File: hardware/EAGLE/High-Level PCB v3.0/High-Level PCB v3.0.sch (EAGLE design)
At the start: 38 parts, among them IC1 DS8921, IC2 DS8921, IC3 MCP2551, J1 Micro-SD, J2 Gyro, J3 Compass, J4 GPS, J5 DB9 Plug, J6 Compass, X1 RJ45, X2 Vehicle control, X4 RJ45

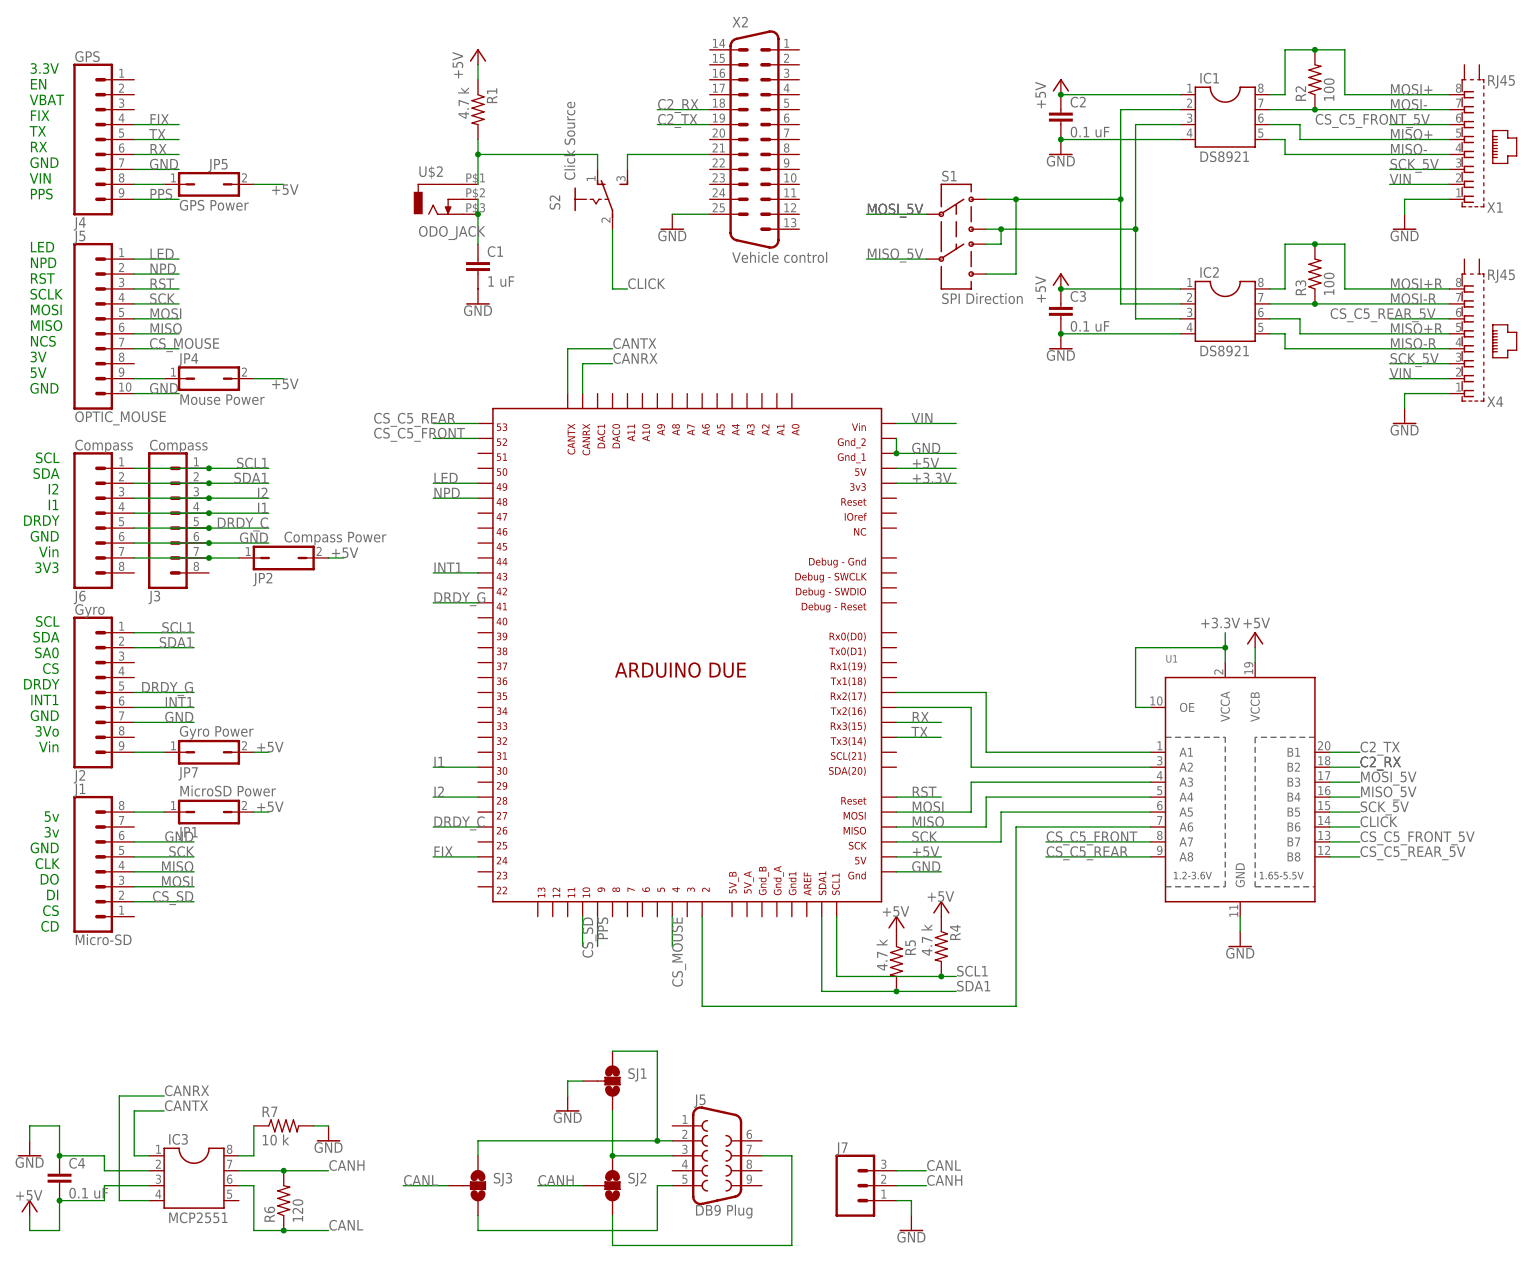
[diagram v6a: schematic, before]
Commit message: Added Test Points
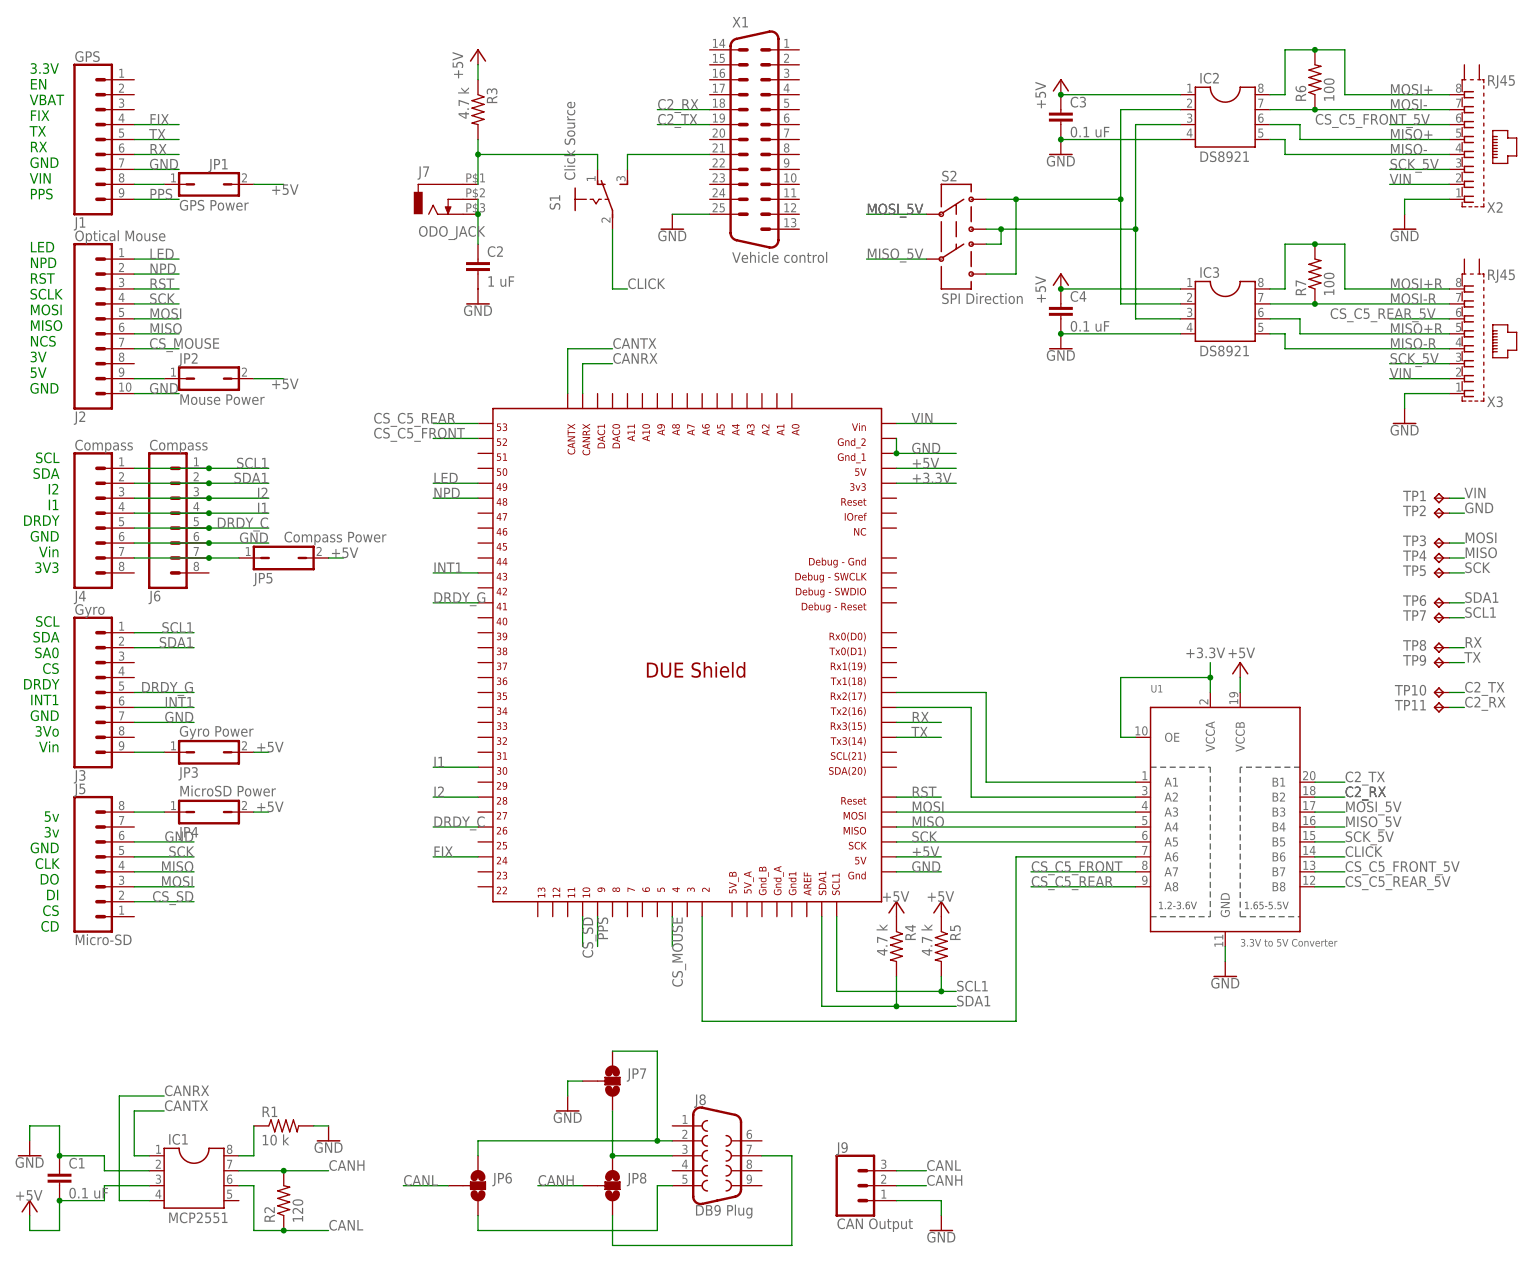
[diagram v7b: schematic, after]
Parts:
- removed OPTIC_MOUSE: J5, SparkFun-Connectors:CONN_10"
- removed SJ1: JUMPER-SMT_3_NO_SILK, SparkFun-Jumpers:JUMPER-SMT_3_NO_SILK
- removed U$2: ODO_JACK, elcanoParts:ODO_JACK
- added J8: DB9 Plug, SparkFun-Connectors:DB9MALE
- added J9: CAN Output, SparkFun-Connectors:CONN_03-SCREW-5MM
- added JP3: Gyro Power, jumper:JP1Q
- added TP1, TP10, TP11, TP2, TP3, TP4, TP5, TP6, TP7, TP8, TP9: TPPAD1-17, testpad:TPPAD1-17
- C1: value 1 uF -> 0.1 uF
- C2: value 0.1 uF -> 1 uF
- IC1: value DS8921 -> MCP2551
- IC3: value MCP2551 -> DS8921
- J1: value Micro-SD -> GPS; device SparkFun-Connectors:CONN_08" -> SparkFun-Connectors:CONN_09
- J2: value Gyro -> Optical Mouse; device SparkFun-Connectors:CONN_09 -> SparkFun-Connectors:CONN_10"
- J3: value Compass -> Gyro; device SparkFun-Connectors:CONN_08" -> SparkFun-Connectors:CONN_09
- J4: value GPS -> Compass; device SparkFun-Connectors:CONN_09 -> SparkFun-Connectors:CONN_08"
- J5: value DB9 Plug -> Micro-SD; device SparkFun-Connectors:DB9MALE -> SparkFun-Connectors:CONN_08"
- J7: value (none) -> ODO_JACK; device SparkFun-Connectors:CONN_03-SCREW-5MM -> elcanoParts:ODO_JACK
- JP1: value MicroSD Power -> GPS Power
- JP2: value Compass Power -> Mouse Power
- JP4: value Mouse Power -> MicroSD Power
- JP5: value GPS Power -> Compass Power
- JP7: value Gyro Power -> JUMPER-SMT_3_NO_SILK; device jumper:JP1Q -> SparkFun-Jumpers:JUMPER-SMT_3_NO_SILK
- R1: value 4.7 k -> 10 k; device resistor:R-US_0204/5 -> rcl:R-US_0204/5
- R2: value 100 -> 120
- R3: value 100 -> 4.7 k; device rcl:R-US_0204/5 -> resistor:R-US_0204/5
- R6: value 120 -> 100
- R7: value 10 k -> 100
- S1: value SPI Direction -> Click Source; device elcanoParts:DPDT_DEV6X5MM_PAC -> switch:255SB
- S2: value Click Source -> SPI Direction; device switch:255SB -> elcanoParts:DPDT_DEV6X5MM_PAC
- U1: value (none) -> 3.3V to 5V Converter
- X1: value RJ45 -> Vehicle control; device con-kycon:GLX-S-88M -> con-subd:M25H
- X2: value Vehicle control -> RJ45; device con-subd:M25H -> con-kycon:GLX-S-88M
- renumbered SJ2 to JP8, SJ3 to JP6, U$1 to MCU1, X4 to X3
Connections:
- removed net N$14 (its old number): J4.8, JP5.1
- new net N$10: J5.8, JP4.1
- net +5V: now also C1.2, C4.1, IC1.3, IC3.1, JP3.2, R3.1; no longer C2.1, C4.2, IC1.1, IC3.3, JP7.2, R1.1
- net C2_RX: now also TP11.TP, X1.18; no longer X2.18
- net C2_TX: now also TP10.TP, X1.19; no longer X2.19
- net CANH: now also IC1.7, J9.2, R2.2; no longer IC3.7, J7.2, R6.2
- net CANL: now also IC1.6, J9.3, R2.1; no longer IC3.6, J7.3, R6.1
- net CANRX: now also IC1.4; no longer IC3.4
- net CANTX: now also IC1.1; no longer IC3.1
- net CLICK: now also S1.P; no longer S2.P
- net CS_C5_FRONT_5V: now also X2.6; no longer X1.6
- net CS_MOUSE: now also J2.7; no longer OPTIC_MOUSE.7
- net CS_SD: now also J5.2; no longer J1.2
- net DRDY_C: now also J4.5; no longer J3.5
- net DRDY_G: now also J3.5; no longer J2.5
- net FIX: now also J1.4; no longer J4.4
- net GND: now also C1.1, C4.2, IC1.2, IC3.4, J1.7, J2.10, J3.7, J4.6, J5.6, J9.1, JP7.2, R1.2, TP2.TP, X1.25, X2.1; no longer C1.2, C4.1, IC1.4, IC3.2, J1.6, J2.7, J3.6, J4.7, J7.1, OPTIC_MOUSE.10, R7.2, SJ1.2, X1.1, X2.25
- net I1: now also J4.4; no longer J3.4
- net I2: now also J4.3; no longer J3.3
- net INT1: now also J3.6; no longer J2.6
- net LED: now also J2.1; no longer OPTIC_MOUSE.1
- net MISO: now also J2.6, J5.4, TP4.TP; no longer J1.4, OPTIC_MOUSE.6
- net MISO+: now also IC2.6, X2.5; no longer IC1.6, X1.5
- net MISO+R: now also IC3.6; no longer IC2.6
- net MISO-: now also IC2.5, X2.4; no longer IC1.5, X1.4
- net MISO-R: now also IC3.5; no longer IC2.5
- net MISO_5V: now also S2.5; no longer S1.5
- net MOSI: now also J2.5, J5.3, TP3.TP; no longer J1.3, OPTIC_MOUSE.5
- net MOSI+: now also IC2.8, R6.2, X2.8; no longer IC1.8, R2.2, X1.8
- net MOSI+R: now also IC3.8, R7.2; no longer IC2.8, R3.2
- net MOSI-: now also IC2.7, R6.1, X2.7; no longer IC1.7, R2.1, X1.7
- net MOSI-R: now also IC3.7, R7.1; no longer IC2.7, R3.1
- net MOSI_5V: now also S2.2; no longer S1.2
- net N$1: now also C2.1, J7.2, J7.3; no longer C1.1, U$2.2, U$2.3
- net N$11: now also J8.3, JP7.3; no longer J5.3, SJ1.3
- net N$13: now also J2.9, JP2.1; no longer JP4.1, OPTIC_MOUSE.9
- net N$15: now also J8.5; no longer J5.5
- net N$16: now also J8.7; no longer J5.7
- net N$17: now also IC1.8, R1.1; no longer IC3.8, R7.1
- net N$18: now also J8.2, JP7.1; no longer J5.2, SJ1.1
- net N$2: now also IC3.2, S2.1, S2.6; no longer IC1.2, S1.1, S1.6
- net N$3: now also IC3.3, S2.3, S2.4; no longer IC1.3, S1.3, S1.4
- net N$6: now also S1.S, X1.21; no longer S2.S, X2.21
- net N$7: now also J7.1, R3.2, S1.O; no longer R1.2, S2.O, U$2.1
- net N$8: now also J4.7, JP5.1; no longer J3.7, JP2.1
- net N$9: now also J3.9, JP3.1; no longer J2.9, JP7.1
- net NPD: now also J2.2; no longer OPTIC_MOUSE.2
- net PPS: now also J1.9; no longer J4.9
- net RST: now also J2.3; no longer OPTIC_MOUSE.3
- net RX: now also J1.6, TP8.TP; no longer J4.6
- net SCK: now also J2.4, J5.5, TP5.TP; no longer J1.5, OPTIC_MOUSE.4
- net SCK_5V: now also X2.3; no longer X1.3
- net SCL1: now also J4.1, R5.2, TP7.TP; no longer J2.1, R4.2
- net SDA1: now also J4.2, R4.2, TP6.TP; no longer J2.2, R5.2
- net TX: now also J1.5, TP9.TP; no longer J4.5
- net VIN: now also TP1.TP, X2.2; no longer X1.2
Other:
- moved on the sheet: C1, C2, C3, C4, IC1, IC2, IC3, J6, JP1, JP2, JP4, JP5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

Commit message: Added some changes (see description)
Added EN for GPS
Added CD for microSD
Cleaned up breakout headers
Need to connect solder jumpers
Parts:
- removed J3: Gyro, SparkFun-Connectors:CONN_09
- removed J6: Compass, SparkFun-Connectors:CONN_08"
- added J10: GPS, SparkFun-Connectors:CONN_09
- added J11: Compass, SparkFun-Connectors:CONN_08"
- added JP10: JUMPER-SMT_2_NO_SILK, SparkFun-Jumpers:JUMPER-SMT_2_NO_SILK
- added JP11, JP12: JUMPER-SMT_3_NO_SILK, SparkFun-Jumpers:JUMPER-SMT_3_NO_SILK
- added JP9: Compass Power, jumper:JP1Q
- added R8: 4.7 k, resistor:R-US_0204/5
- J1: value GPS -> Optical Mouse; device SparkFun-Connectors:CONN_09 -> SparkFun-Connectors:CONN_10"
- J2: value Optical Mouse -> Compass; device SparkFun-Connectors:CONN_10" -> SparkFun-Connectors:CONN_08"
- J4: value Compass -> Gyro; device SparkFun-Connectors:CONN_08" -> SparkFun-Connectors:CONN_09
- JP3: value Gyro Power -> JUMPER-SMT_2_NO_SILK; device jumper:JP1Q -> SparkFun-Jumpers:JUMPER-SMT_2_NO_SILK
- JP5: value Compass Power -> Gyro Power
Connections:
- removed net +3.3V: MCU1.3V3, U1.OE, U1.VCCA
- new net +3V3: JP1.2, MCU1.3V3, R8.1, U1.OE, U1.VCCA
- new net CARD_DETECT: J5.8, MCU1.11, R8.2
- new net EN: J10.8, MCU1.13
- new net N$19: J4.6, JP10.1
- new net N$20: J4.7, JP3.1
- new net N$21: J4.8, JP11.2
- new net N$22: J4.9, JP12.2
- net +5V: now also JP9.2; no longer JP1.2, JP3.2
- net CS_MOUSE: now also J1.4; no longer J2.7
- net CS_SD: now also J5.7; no longer J5.2
- net DRDY_C: now also J11.4, J2.4; no longer J4.5, J6.5
- net DRDY_G: now also J4.5; no longer J3.5
- net FIX: now also J10.6; no longer J1.4
- net GND: now also J1.1, J10.3, J11.3, J2.3, J4.3, J5.3; no longer J1.7, J2.10, J3.7, J4.6, J5.6, J6.6
- net I1: now also J11.5, J2.5; no longer J4.4, J6.4
- net I2: now also J11.6, J2.6; no longer J4.3, J6.3
- net INT1: now also J4.4; no longer J3.6
- net LED: now also J1.10; no longer J2.1
- net MISO: now also J1.5, J5.5; no longer J2.6, J5.4
- net MOSI: now also J1.6, J5.6; no longer J2.5, J5.3
- net N$10: now also J5.1; no longer J5.8
- net N$13: now also J1.2; no longer J2.9
- net N$14: now also J10.2; no longer J1.8
- net N$8: now also J11.2, J2.2, JP9.1; no longer J4.7, J6.7, JP5.1
- net N$9: now also J4.1, JP5.1; no longer J3.9, JP3.1
- net NPD: now also J1.9; no longer J2.2
- net PPS: now also J10.1; no longer J1.9
- net RST: now also J1.8; no longer J2.3
- net RX: now also J10.4; no longer J1.6
- net SCK: now also J1.7, J5.4; no longer J2.4, J5.5
- net SCL1: now also J11.8, J2.8; no longer J3.1, J4.1, J6.1
- net SDA1: now also J11.7, J2.7; no longer J3.2, J4.2, J6.2
- net TX: now also J10.5; no longer J1.5
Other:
- note added: "CD CS DI DO CLK GND 3v 5v"
- note removed: "5v 3v GND CLK DO DI CS CD"
- moved on the sheet: J5, JP1, JP2, JP4, JP5
